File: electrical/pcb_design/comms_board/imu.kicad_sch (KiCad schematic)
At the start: 19 parts, among them U2 BMI323, U3 BMI323

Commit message: First draft of Cheerful Coffee comms board
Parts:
- removed R16, R17: 9k31, footprints:Nondescript_R_0402_1005Metric, symbol Device:R
- removed R19, R20, R32, R33: 33, footprints:Nondescript_R_0402_1005Metric, symbol Device:R
- added C17, C18, C21, C22, C23, C25: 100n, footprints:Nondescript_C_0402_1005Metric, symbol Device:C
- added C19, C20, C24: 1u, footprints:Nondescript_C_0402_1005Metric, symbol Device:C
- added R23: 33, footprints:Nondescript_R_0402_1005Metric, symbol Device:R
- added R34: 9k31, footprints:Nondescript_R_0402_1005Metric, symbol Device:R
- added U5: MAGNETOMETER, footprints:QFN50P300X300X100-17N-D, symbol TVSC:MLX90393ELW-ABA-011-RE
- U6: renamed from U3; value BMI323 -> IMU1
- U7: renamed from U2; value BMI323 -> IMU2
- renumbered R18 to R24, R34 to R26, R35 to R27, R21 to R28, R41 to R30, R40 to R31, R37 to R32, R38 to R33, R36 to R35, R39 to R36
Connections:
- net +3V3: now also C17.1, C18.1, C19.1, C20.1, C21.1, C22.1, C23.1, C24.1, C25.1, U5.15 (VDD), U5.8 (VDD_IO)
- net GND: now also C17.2, C18.2, C19.2, C20.2, C21.2, C22.2, C23.2, C24.2, C25.2, R34.2, U5.10 (N/C_3), U5.11 (A1), U5.12 (A0), U5.13 (VSS), U5.14 (N/C_4), U5.16 (N/C_5), U5.17 (EP), U5.4 (N/C_1), U5.7 (INT/TRIG), U5.9 (N/C_2)
- net IMU1_SPI_CS: now also U6.12 (CSB)
- net IMU2_SPI_CS: now also U7.12 (CSB)
- net SPI_SCK: now reaches U6.13 (SCx), U7.13 (SCx)
- net SPI_SCK: now also U5.3 (SCL/SCLK)
- net SPI_MOSI: now reaches U6.14 (SDx), U7.14 (SDx)
- net SPI_MOSI: now also U5.5 (SDA/MOSI)
- net SPI3_MISO renamed SPI_MISO
- net SPI_MISO: now also R23.2
- new net: R23.1, U5.6 (MISO)
- new net IMU_MAG_INT1: R34.1, U5.1 (INT)
- new net IMU_MAG_SPI_CS: U5.2 (SENB/CS)
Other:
- moved on the sheet: R22, R24, R26, R27, R28, R30, R31, R32, R33, R35, R36, U6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

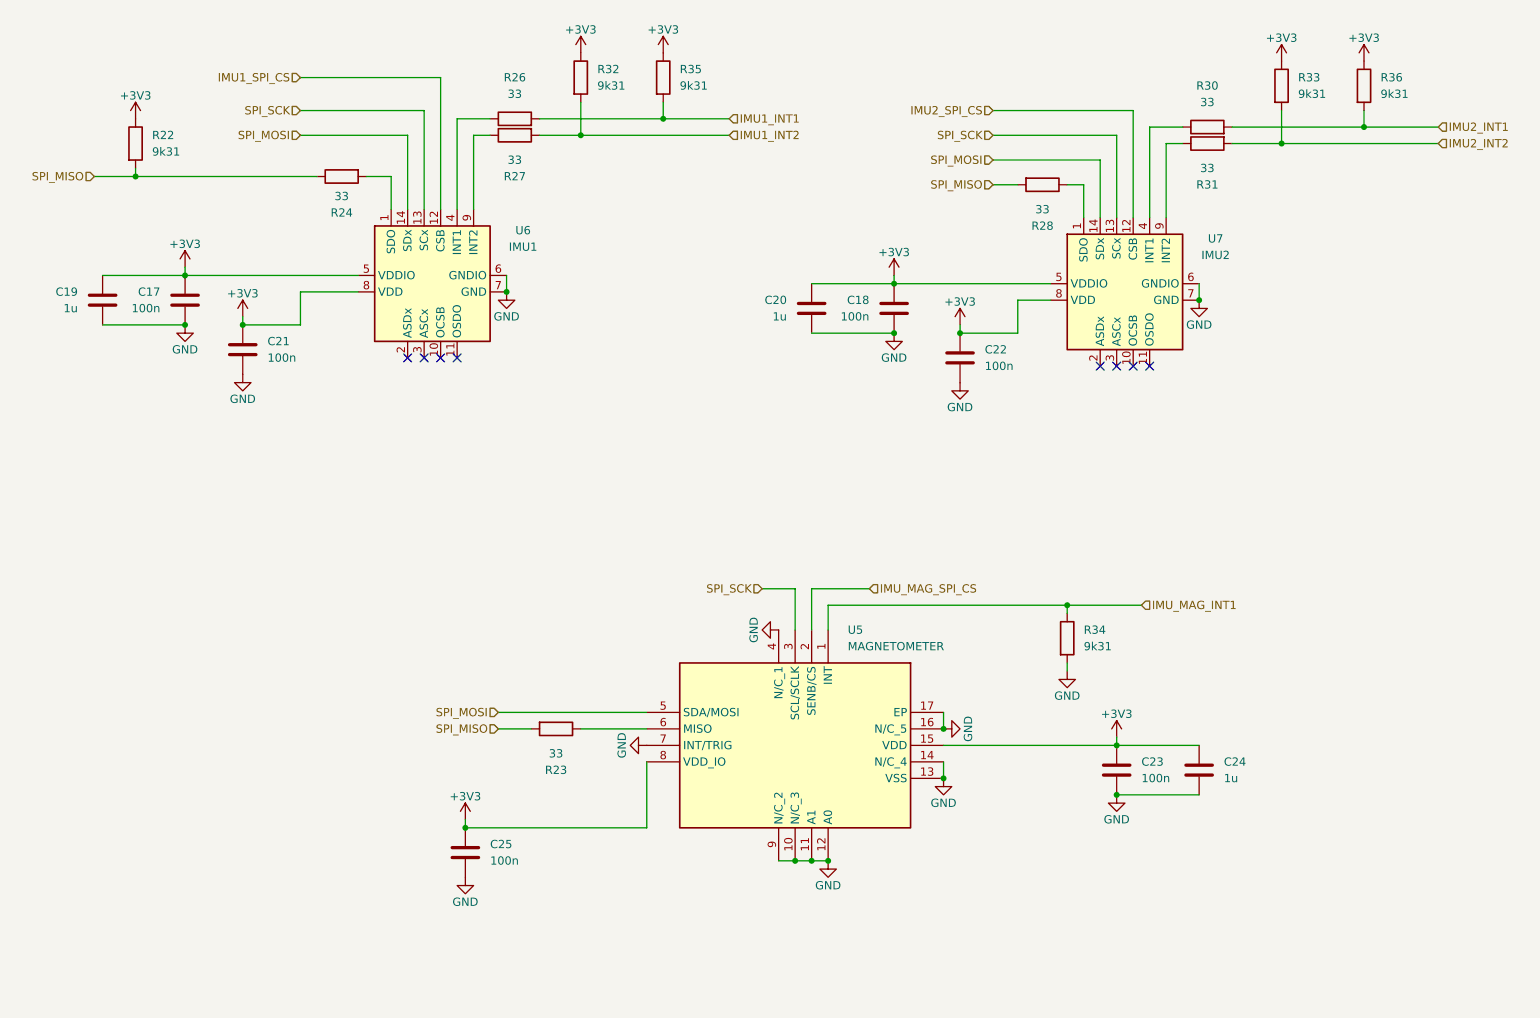
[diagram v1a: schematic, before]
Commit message: Add an IMU to the comms board. This IMU will make it possible to use the comms board as a gesture-based remote control.
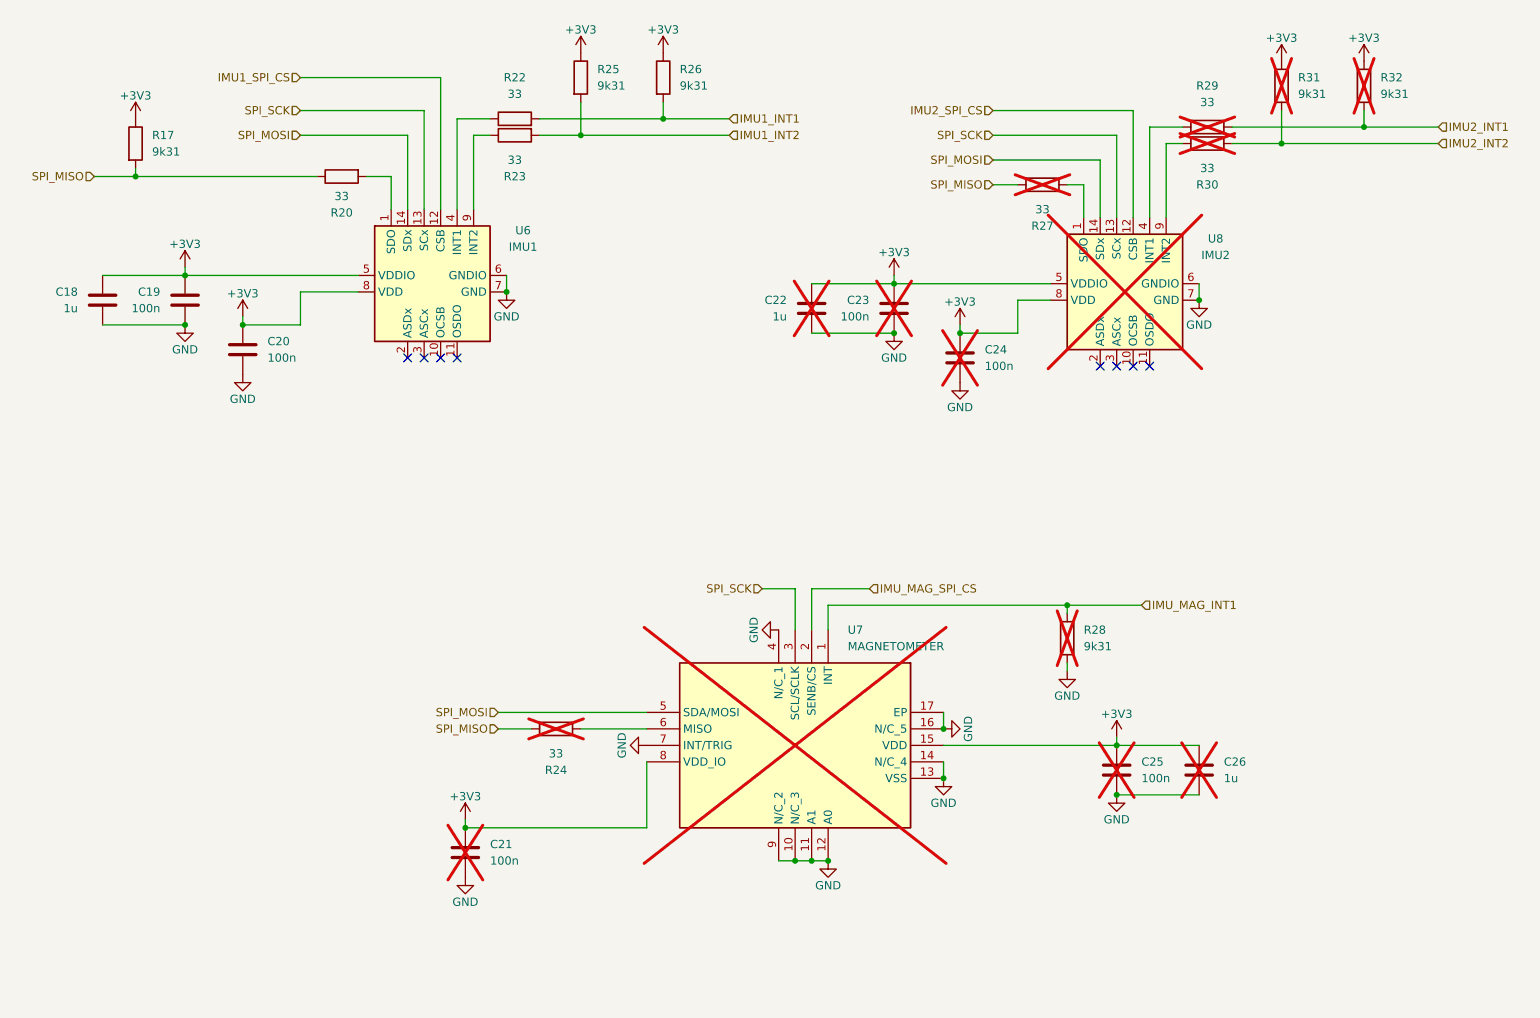
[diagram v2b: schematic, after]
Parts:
- C21: renamed from C25; now not fitted; now left out of the parts list
- C22: renamed from C20; now not fitted; now left out of the parts list
- C23: renamed from C18; now not fitted; now left out of the parts list
- C24: renamed from C22; now not fitted; now left out of the parts list
- C25: renamed from C23; now not fitted; now left out of the parts list
- C26: renamed from C24; now not fitted; now left out of the parts list
- R24: renamed from R23; now not fitted; now left out of the parts list
- R27: renamed from R28; now not fitted; now left out of the parts list
- R28: renamed from R34; now not fitted; now left out of the parts list
- R29: renamed from R30; now not fitted; now left out of the parts list
- R30: renamed from R31; now not fitted; now left out of the parts list
- R31: renamed from R33; now not fitted; now left out of the parts list
- R32: renamed from R36; now not fitted; now left out of the parts list
- U7: renamed from U5; now not fitted; now left out of the parts list
- U8: renamed from U7; now not fitted; now left out of the parts list
- renumbered C19 to C18, C17 to C19, C21 to C20, R22 to R17, R24 to R20, R26 to R22, R27 to R23, R32 to R25, R35 to R26
